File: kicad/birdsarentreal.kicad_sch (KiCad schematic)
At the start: 7 parts, among them U10 DRV8833PW, U11 L7806, U12 NCP176AMX330TCG, U6 ESP32-DEVKITC, U8 GY-521, U9 MCP73831-2-OT

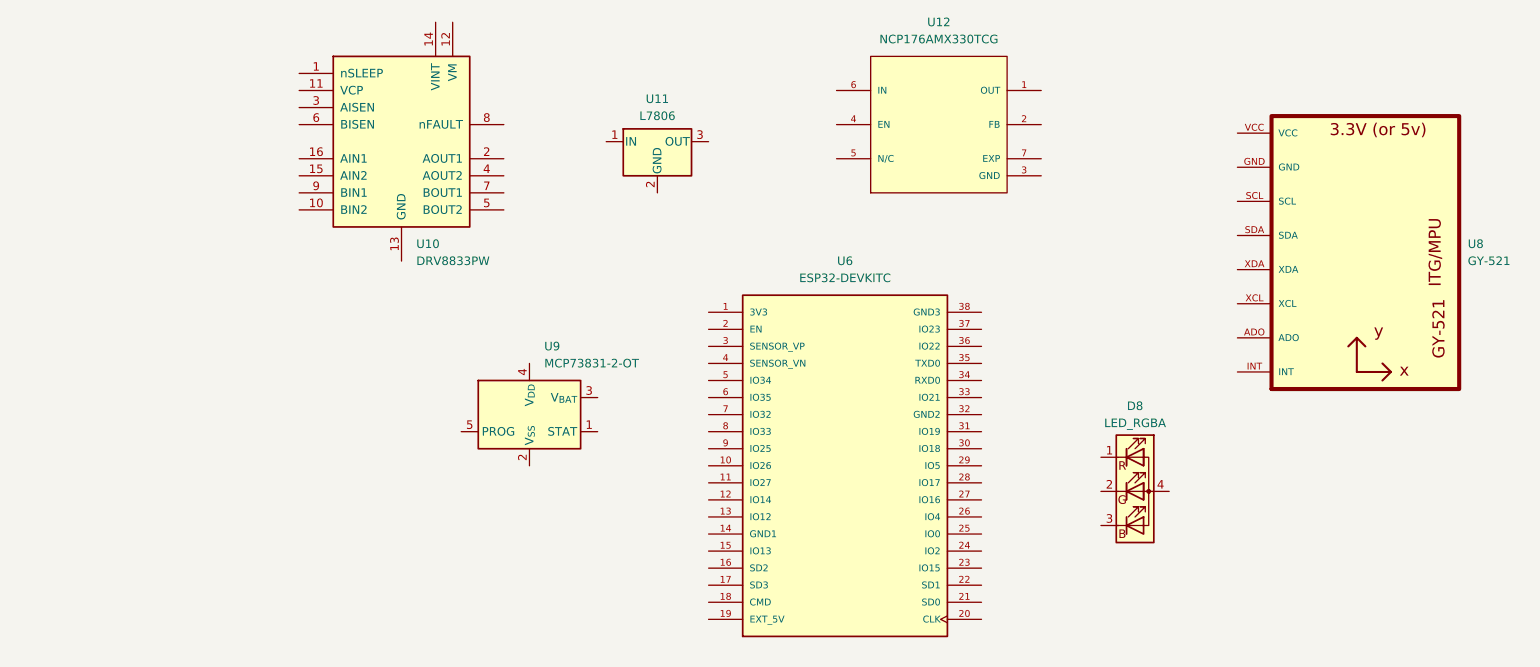
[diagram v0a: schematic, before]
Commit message: Finish Robot Schematic
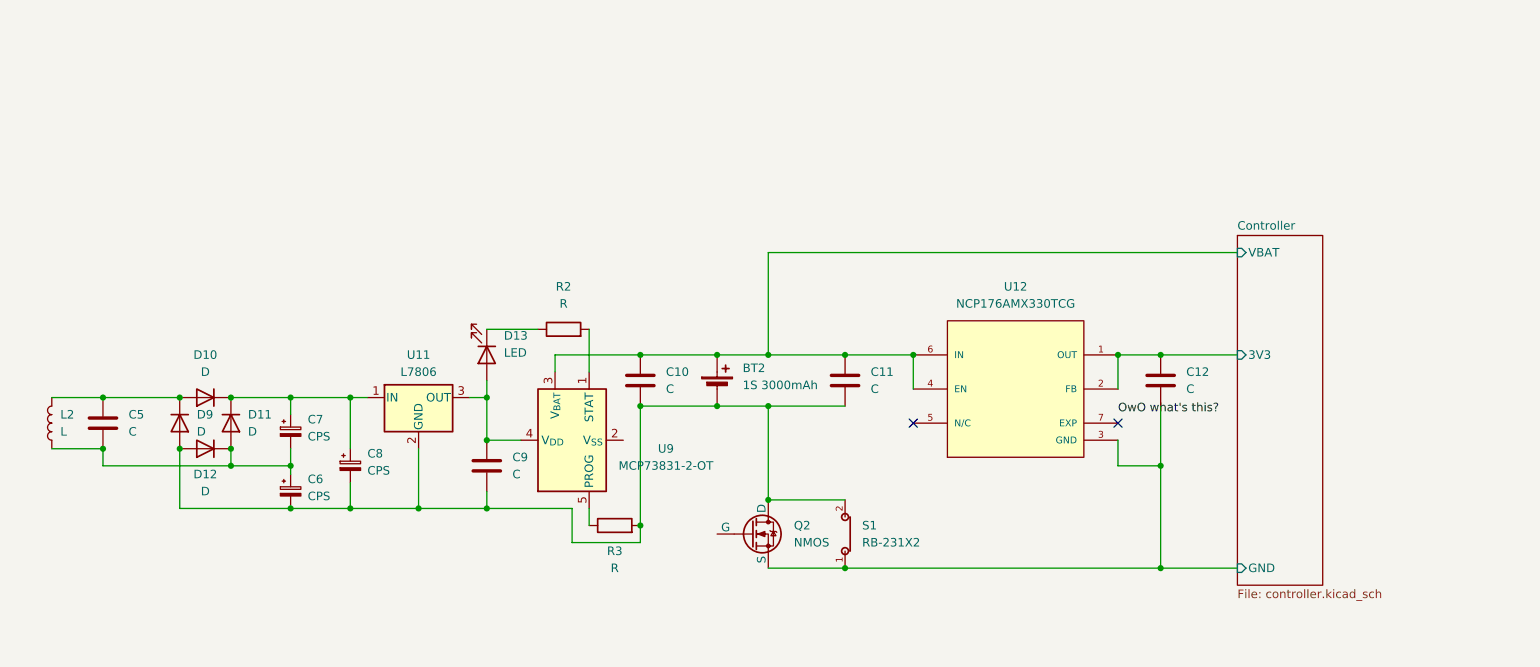
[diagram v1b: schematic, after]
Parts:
- removed D8: LED_RGBA, symbol Device:LED_RGBA
- removed U10: DRV8833PW, Package_SO:TSSOP-16_4.4x5mm_P0.65mm, symbol Driver_Motor:DRV8833PW
- removed U6: ESP32-DEVKITC, ESP32-DEVKITC:MODULE_ESP32-DEVKITC, symbol ESP32DEV:ESP32-DEVKITC
- removed U8: GY-521, GY-521:GY-521, symbol GY-521:GY-521
- added BT2: 1S 3000mAh, symbol Device:Battery_Cell
- added C10, C11, C12, C5, C9: C, symbol Device:C
- added C6, C7, C8: CPS, symbol Device:C_Polarized_Small
- added D10, D11, D12, D9: D, symbol Device:D
- added D13: LED, symbol Device:LED
- added L2: L, symbol Device:L
- added Q2: NMOS, symbol Simulation_SPICE:NMOS
- added R2, R3: R, symbol Device:R
- added S1: RB-231X2, RB-231X2:SW_RB-231X2, symbol RB-231X2:RB-231X2
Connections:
- net at U11.1 (IN): now also C7.1, C8.1, D10.1 (K), D11.1 (K)
- net at U11.2 (GND): now also BT2.2 (-), C10.2, C11.2, C6.2, C8.2, C9.2, D12.2 (A), D9.2 (A), Q2.1 (D), R3.2, S1.2
- net at U11.3 (OUT): now also U9.4 (V_{DD}), C9.1, D13.2 (A)
- net at U9.1 (STAT): now also R2.2
- net Controller/VBAT: now reaches U9.3 (V_{BAT})
- net Controller/VBAT: now also U12.4 (EN), U12.6 (IN), BT2.1 (+), C10.1, C11.1
- net at U9.5 (PROG): now also R3.1
- net Controller/3V3: now reaches U12.1 (OUT)
- net Controller/3V3: now also U12.2 (FB), C12.1
- net Controller/GND: now reaches U12.3 (GND)
- net Controller/GND: now also C12.2, Q2.3 (S), S1.1
- new net: D13.1 (K), R2.1
- new net: C5.2, C6.1, C7.2, D11.2 (A), D12.1 (K), L2.1
- new net: C5.1, D10.2 (A), D9.1 (K), L2.2
- no-connect marks 0 -> 2
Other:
- added sheet Controller (controller.kicad_sch)
- moved on the sheet: U11, U12, U9

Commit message: Add capacitors
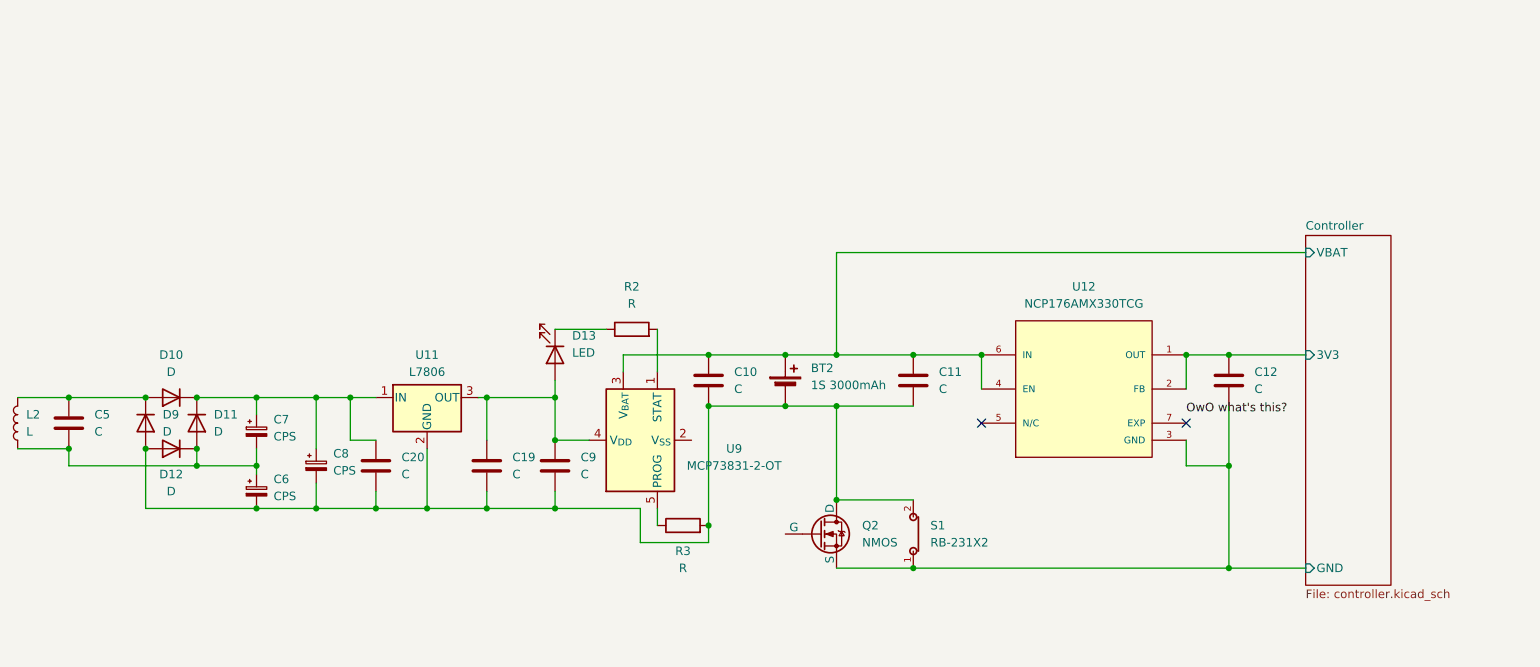
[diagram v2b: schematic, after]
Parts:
- added C19, C20: C, symbol Device:C
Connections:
- net at C9.1, D13.2 (A), U11.3 (OUT)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: now also C19.1
- net at BT2.2 (-), C10.2, C11.2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: now also C19.2, C20.2
- net at C7.1, C8.1, D10.1 (K)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: now also C20.1
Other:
- moved on the sheet: BT2, C10, C11, C12, C5, C6, C7, C8, C9, D10, D11, D12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

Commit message: Add all symbols and values
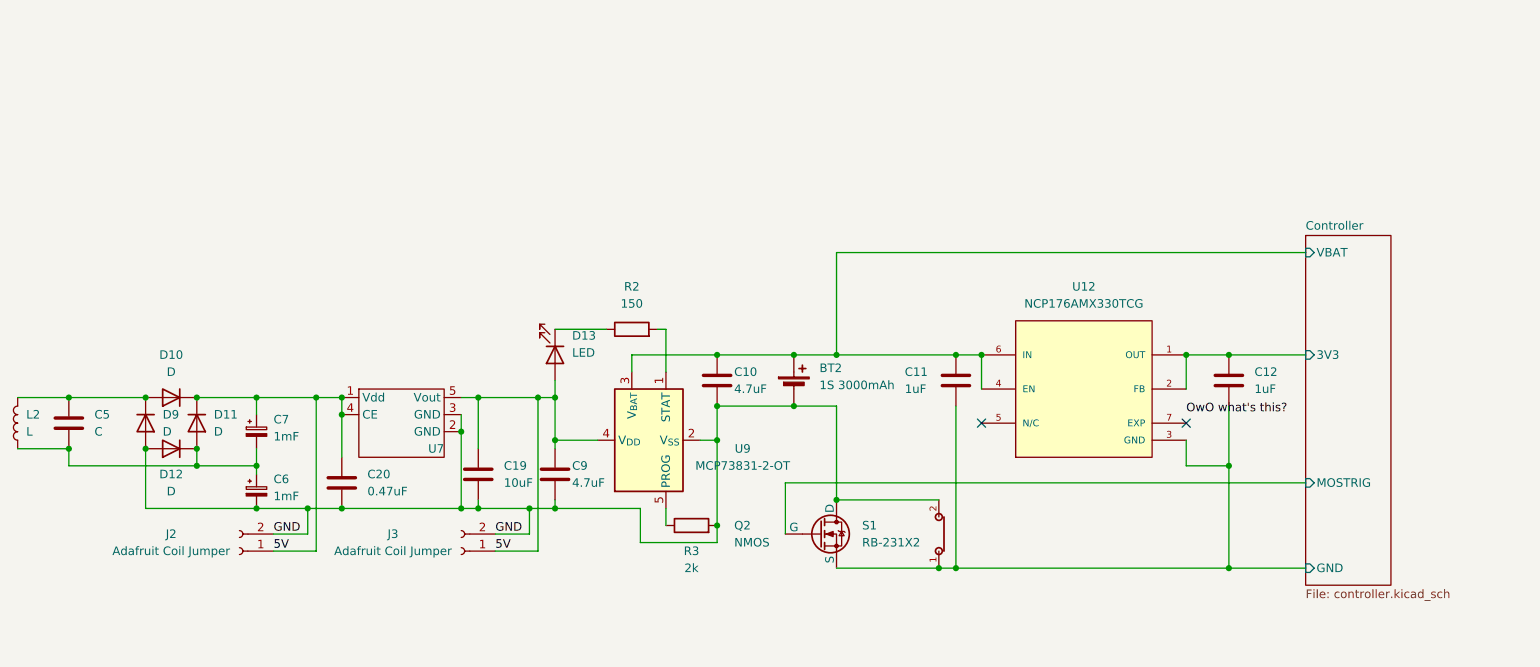
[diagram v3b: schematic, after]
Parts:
- removed C8: CPS, symbol Device:C_Polarized_Small
- removed U11: L7806, Package_TO_SOT_SMD:TO-263-3_TabPin2, symbol Regulator_Linear:L7806
- added J2, J3: Adafruit Coil Jumper, Connector_PinHeader_1.00mm:PinHeader_1x02_P1.00mm_Vertical, symbol Connector:Conn_01x02_Socket
- added U7: ~, Package_TO_SOT_SMD:SOT-89-5, symbol R1500H050B:R1500H050B
- C10, C9: value C -> 4.7uF; footprint (none) -> Capacitor_SMD:C_0805_2012Metric
- C11, C12: value C -> 1uF; footprint (none) -> Capacitor_SMD:C_0805_2012Metric
- C19: value C -> 10uF; footprint (none) -> Capacitor_SMD:C_0805_2012Metric
- C20: value C -> 0.47uF; footprint (none) -> Capacitor_SMD:C_0805_2012Metric
- C5: footprint (none) -> Capacitor_THT:CP_Radial_D10.0mm_P5.00mm
- C6, C7: value CPS -> 1mF; footprint (none) -> Capacitor_THT:CP_Radial_D10.0mm_P5.00mm
- D10, D11, D12, D9: footprint (none) -> Diode_SMD:D_0805_2012Metric
- D13: footprint (none) -> LED_SMD:LED_0805_2012Metric
- L2: footprint (none) -> Connector_PinHeader_1.00mm:PinHeader_1x02_P1.00mm_Vertical
- Q2: footprint (none) -> Package_TO_SOT_SMD:SOT-323_SC-70
- R2: value R -> 150; footprint (none) -> Resistor_SMD:R_0805_2012Metric
- R3: value R -> 2k; footprint (none) -> Resistor_SMD:R_0805_2012Metric
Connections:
- net Controller/GND: now also C11.1
- net Controller/VBAT: now also C11.2; no longer C11.1
- net 5V: now reaches C19.1, C9.1, D13.2 (A), U9.4 (V_{DD})
- net 5V: now also C20.1, C7.1, D10.1 (K), D11.1 (K), J2.1 (Pin_1), J3.1 (Pin_1), U7.1 (Vdd), U7.4 (CE), U7.5 (Vout)
- net GND: now reaches BT2.2 (-), C10.2, C19.2, C20.2, C6.2, C9.2, D12.2 (A), D9.2 (A), Q2.1 (D), R3.2, S1.2
- net GND: now also U9.2 (V_{SS}), J2.2 (Pin_2), J3.2 (Pin_2), U7.2 (GND), U7.3 (GND); no longer C11.2
- net Controller/MOSTRIG: now reaches Q2.2 (G)
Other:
- sheet Controller ports: added MOSTRIG; removed none
- moved on the sheet: BT2, C10, C11, C19, C20, C9, R3, S1, U9

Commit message: Fix footprints
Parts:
- BT2: footprint (none) -> Connector_JST:JST_GH_BM02B-GHS-TBT_1x02-1MP_P1.25mm_Vertical
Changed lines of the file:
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@@
       (effects (font (size 1.27 1.27)) (justify left))
     )
-    (property "Footprint" "" (at 129.54 82.296 90)
+    (property "Footprint" "Connector_JST:JST_GH_BM02B-GHS-TBT_1x02-1MP_P1.25mm_Vertical" (at 129.54 82.296 90)
       (effects (font (size 1.27 1.27)) hide)
     )
@@
         )
         (path "/9f6eb88e-d254-4b8d-b64f-838940a89234/50902c9c-c184-4e8b-b7c8-1add935d161c"
-          (reference "R1500H050B") (unit 1)
+          (reference "R1500H050B1") (unit 1)
         )
       )

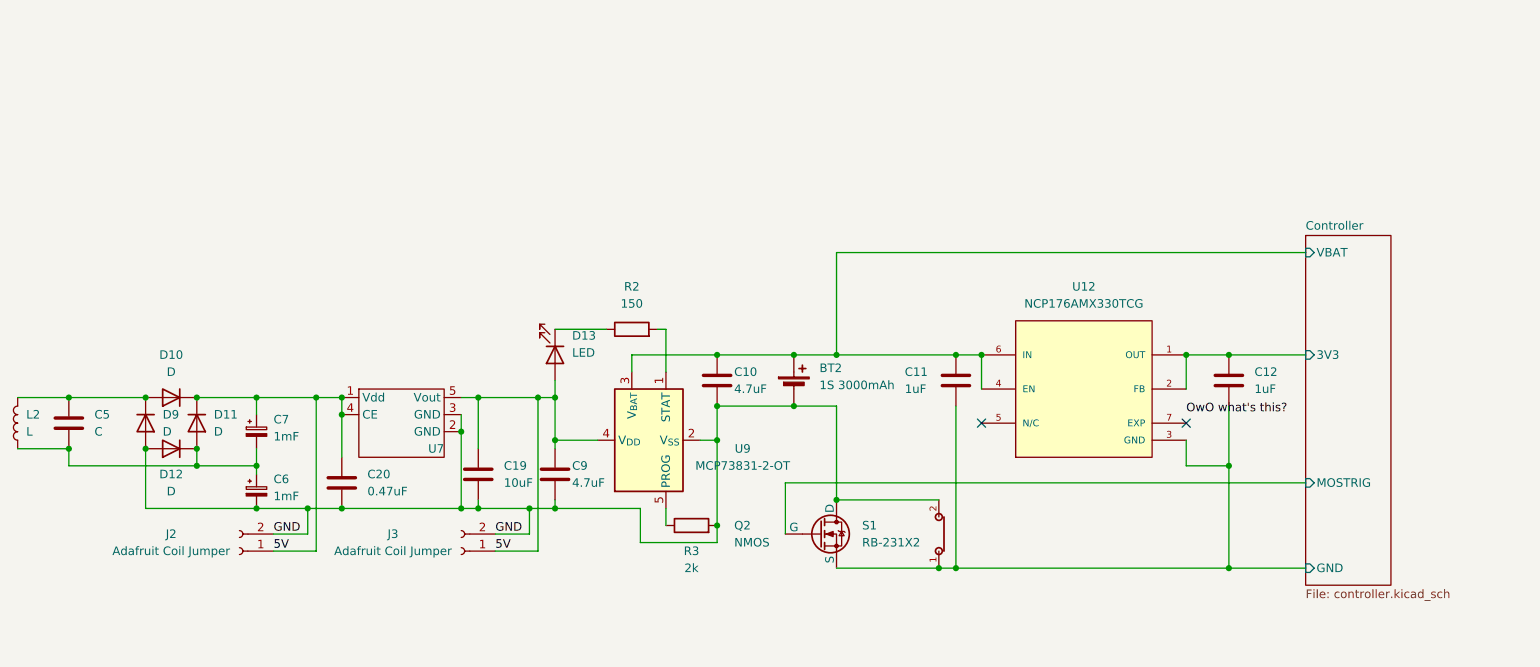
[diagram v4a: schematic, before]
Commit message: Add board layout
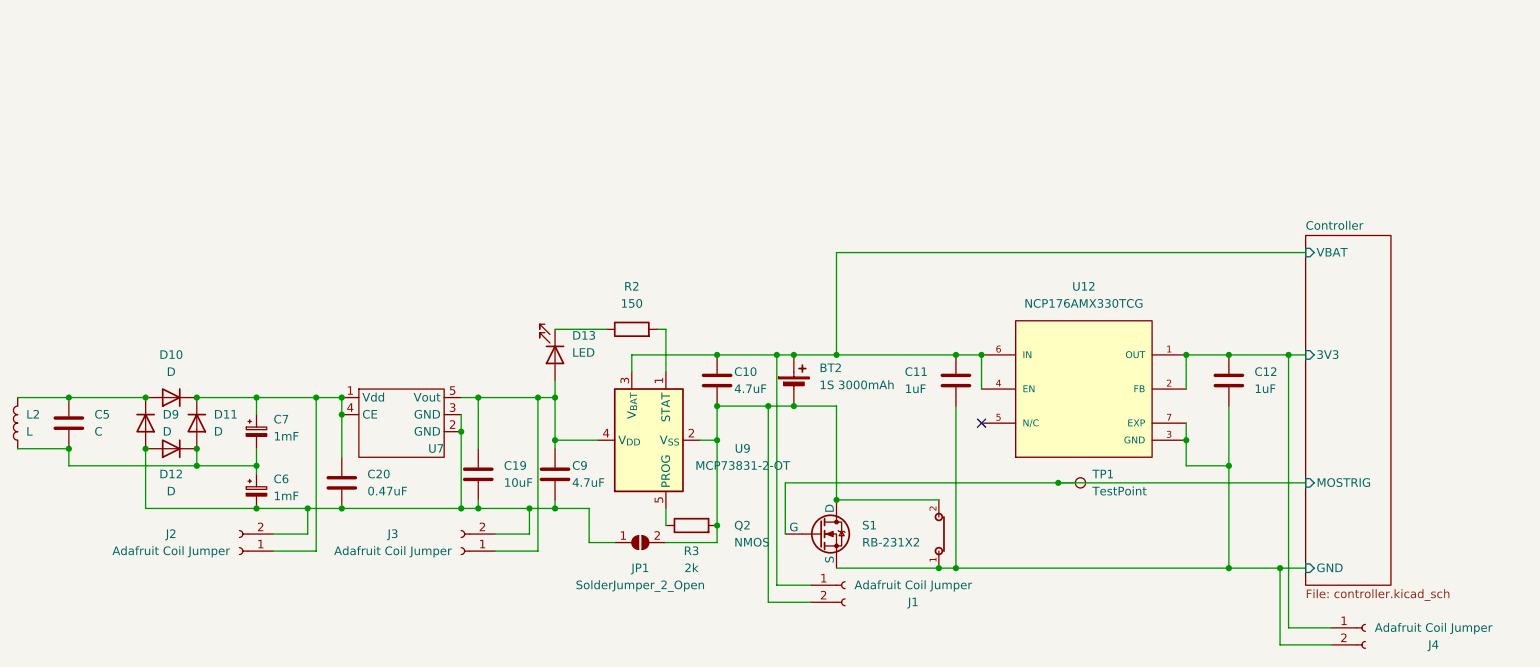
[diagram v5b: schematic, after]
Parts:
- added J1, J4: Adafruit Coil Jumper, Connector_PinHeader_1.00mm:PinHeader_1x02_P1.00mm_Vertical, symbol Connector:Conn_01x02_Socket
- added JP1: SolderJumper_2_Open, Diode_SMD:D_0805_2012Metric_Pad1.15x1.40mm_HandSolder, symbol Jumper:SolderJumper_2_Open
- added TP1: TestPoint, TestPoint:TestPoint_Pad_D2.0mm, symbol Connector:TestPoint
- C10, C11, C12, C19, C20, C9: footprint Capacitor_SMD:C_0805_2012Metric -> Capacitor_SMD:C_0805_2012Metric_Pad1.18x1.45mm_HandSolder
- D10, D11, D12, D9: footprint Diode_SMD:D_0805_2012Metric -> Diode_SMD:D_0805_2012Metric_Pad1.15x1.40mm_HandSolder
- D13: footprint LED_SMD:LED_0805_2012Metric -> LED_SMD:LED_0805_2012Metric_Pad1.15x1.40mm_HandSolder
- Q2: footprint Package_TO_SOT_SMD:SOT-323_SC-70 -> Package_TO_SOT_SMD:SOT-323_SC-70_Handsoldering
- R2, R3: footprint Resistor_SMD:R_0805_2012Metric -> Resistor_SMD:R_0805_2012Metric_Pad1.20x1.40mm_HandSolder
- U9: footprint Package_TO_SOT_SMD:SOT-23-5 -> Package_TO_SOT_SMD:SOT-23-5_HandSoldering
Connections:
- net Controller/3V3: now also J4.1 (Pin_1)
- net Controller/GND: now also U12.7 (EXP), J4.2 (Pin_2)
- net Controller/MOSTRIG: now also TP1.1
- net Controller/VBAT: now also J1.1 (Pin_1)
- net 5V: no longer names the net of C20.1, C7.1, D10.1 (K), D11.1 (K), J2.1 (Pin_1), U7.1 (Vdd), U7.4 (CE)
- net 5V: no longer C19.1, C9.1, D13.2 (A), J3.1 (Pin_1), U7.5 (Vout), U9.4 (V_{DD})
- net GND: no longer names the net of C19.2, C20.2, C6.2, C9.2, D12.2 (A), D9.2 (A), J2.2 (Pin_2), J3.2 (Pin_2), U7.2 (GND), U7.3 (GND)
- net GND: now also JP1.1 (A); no longer BT2.2 (-), C10.2, Q2.1 (D), R3.2, S1.2, U9.2 (V_{SS})
- new net: C19.1, C9.1, D13.2 (A), J3.1 (Pin_1), U7.5 (Vout), U9.4 (V_{DD})
- new net: BT2.2 (-), C10.2, J1.2 (Pin_2), JP1.2 (B), Q2.1 (D), R3.2, S1.2, U9.2 (V_{SS})
- no-connect marks 2 -> 1
